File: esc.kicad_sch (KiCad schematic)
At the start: 49 parts, among them Q10 NMOS, Q5 NMOS, Q6 NMOS, Q7 NMOS, Q8 NMOS, Q9 NMOS, U16 DRV8328ARUYR, U20 STM32G071GBU6

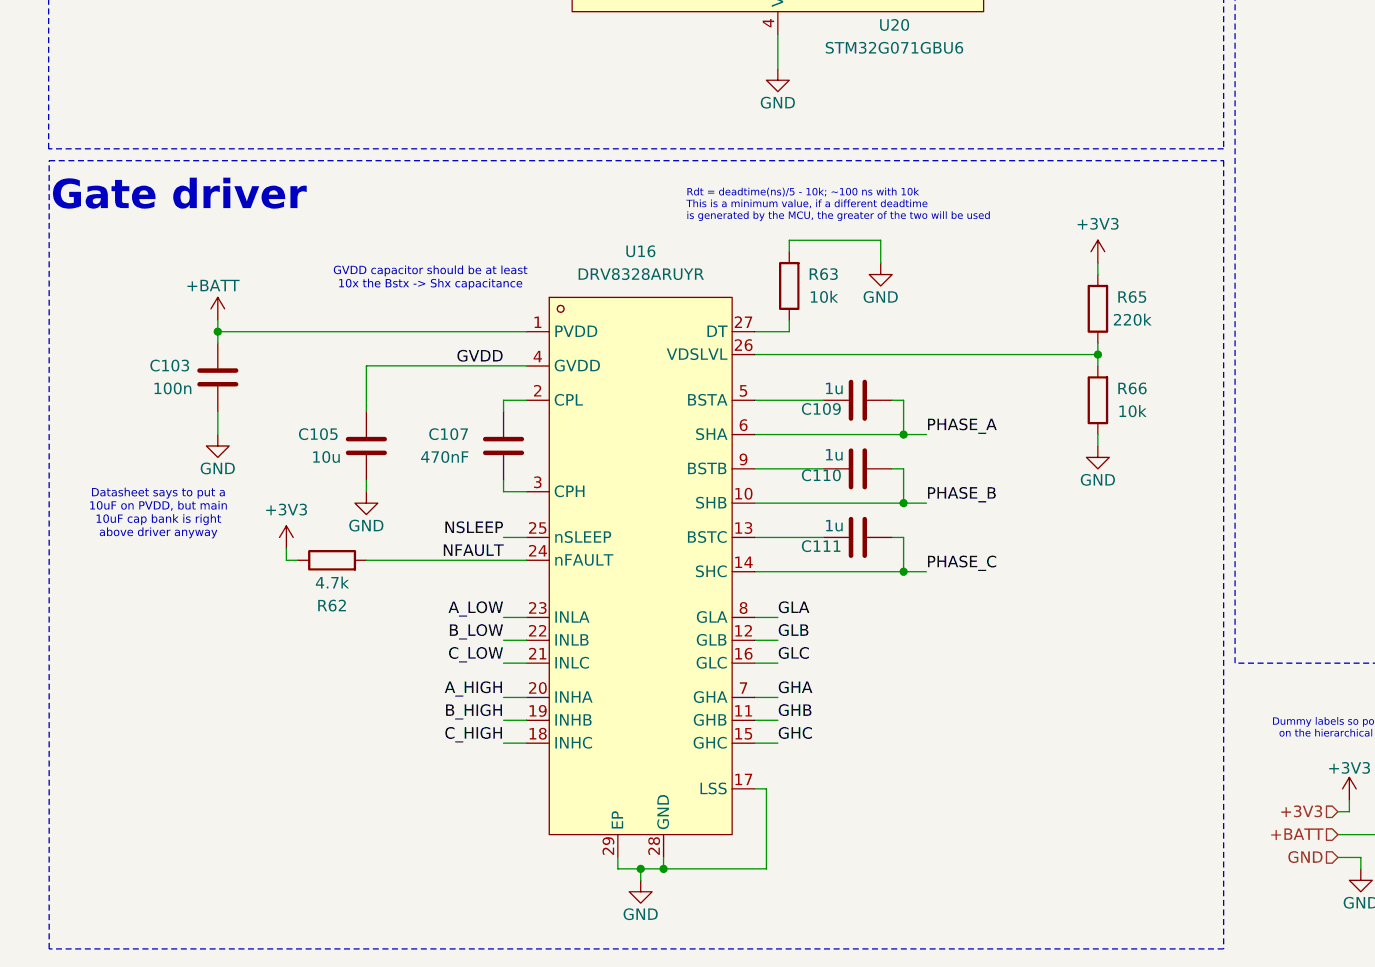
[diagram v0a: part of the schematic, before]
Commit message: Switch to 2.2 uH 1008 inductor for both DCDC converters
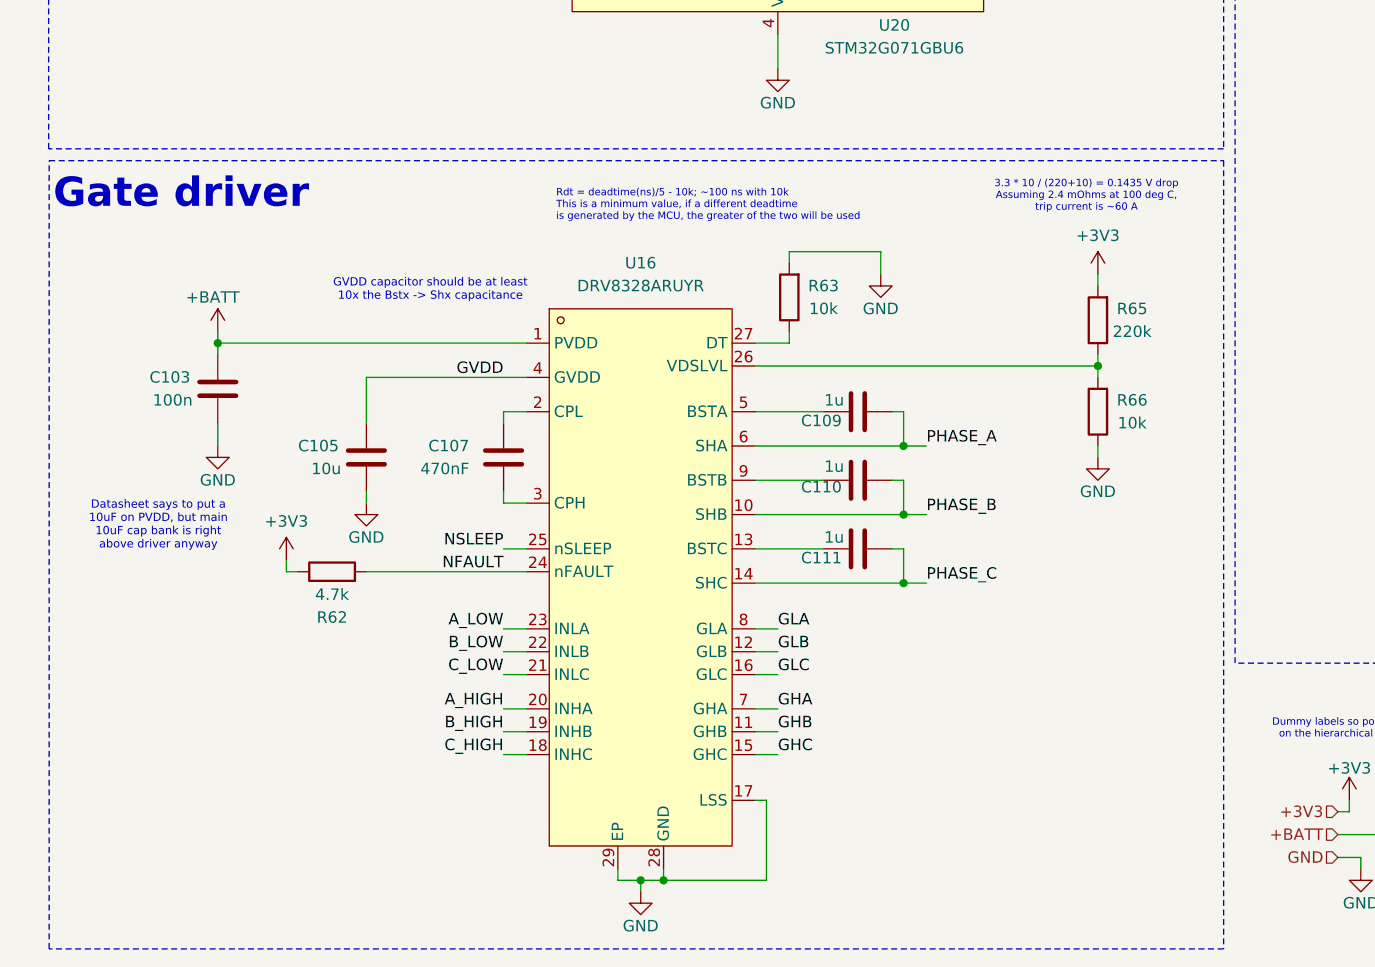
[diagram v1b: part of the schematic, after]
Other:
- note added: "3.3 * 10 / (220+10) = 0.1435 V drop Assuming 2.4 mOhms at 100 deg C, trip current is ~60 A"
- moved on the sheet: C103, C105, C107, C109, C110, C111, R62, R63, R65, R66, U16

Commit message: Fill out most of BOM
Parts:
- C107: LCSC Part (none) -> C576436
- D14: LCSC Part (none) -> C5440628
- Q10, Q5, Q6, Q7, Q8, Q9: LCSC Part (none) -> C2890409
- R136, R62: LCSC Part (none) -> C270346
- R139, R76, R79, R84: LCSC Part (none) -> C270365
- R63, R66, R75, R77, R78, R80, R83, R85: LCSC Part (none) -> C473048
- R65: LCSC Part (none) -> C473458
- R69, R70, R73, R74, R81, R82: LCSC Part (none) -> C270817

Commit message: Finish BOM list
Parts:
- C103: LCSC Part (none) -> C307331
- C105: LCSC Part (none) -> C237493
- C109, C110, C111, C180: LCSC Part (none) -> C52923
- C176, C178: LCSC Part (none) -> C76939

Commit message: Rename project
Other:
- title: Anticopter Duo -> P4eregrine

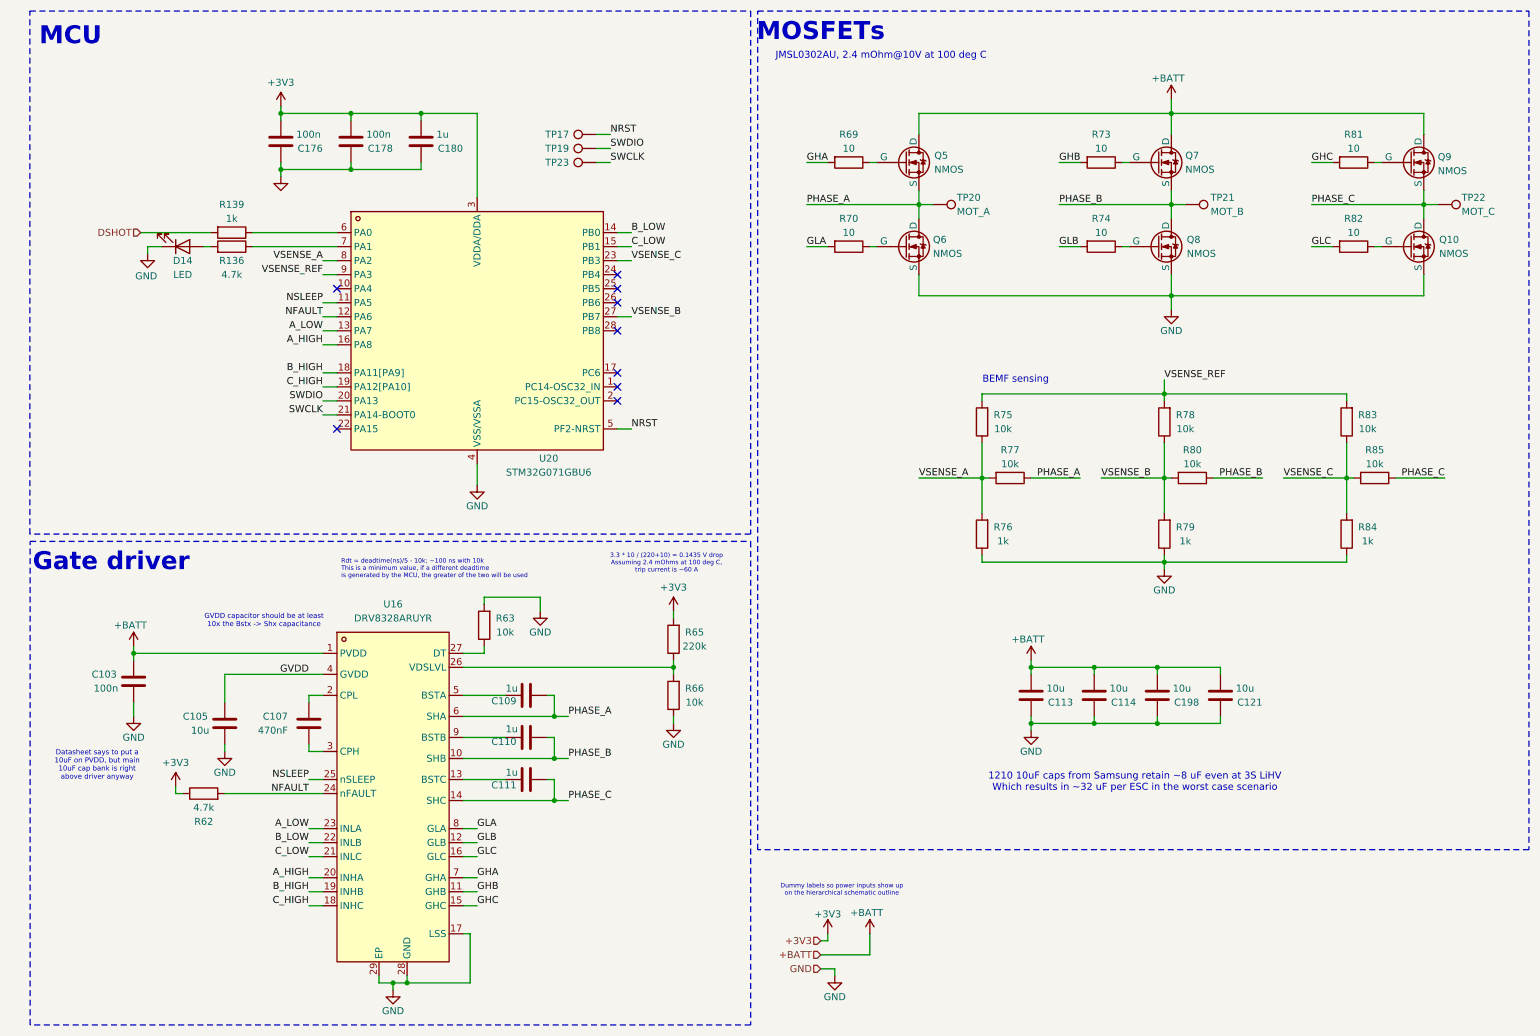
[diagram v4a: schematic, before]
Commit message: Remove redundant 100n STM cap
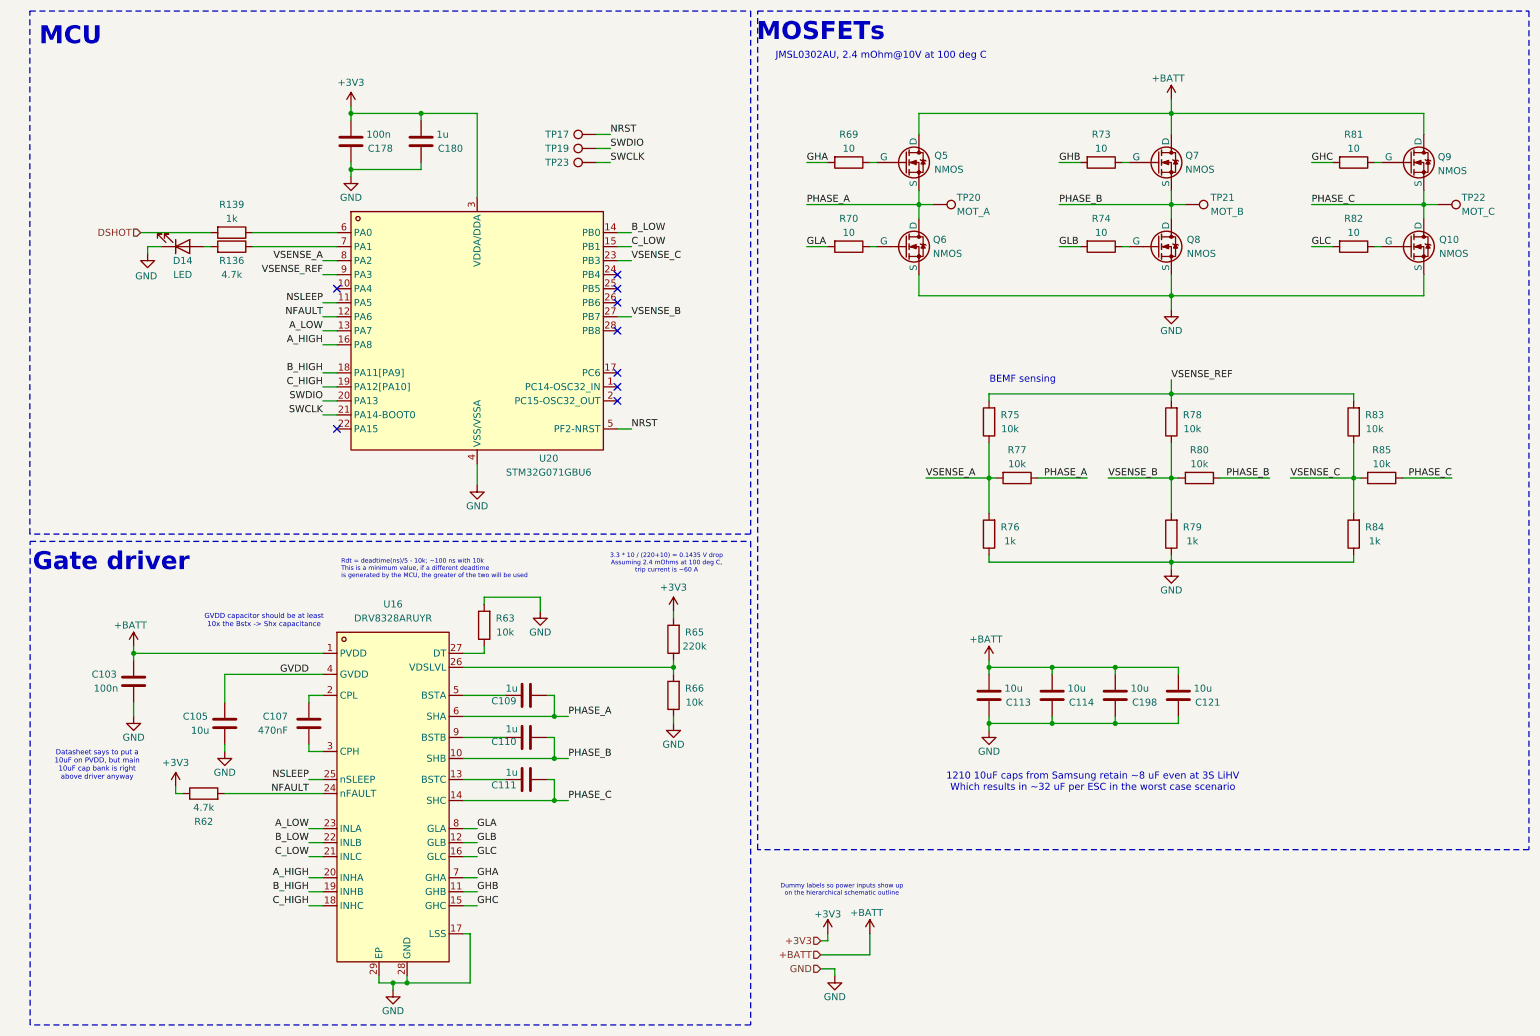
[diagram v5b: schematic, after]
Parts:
- removed C176: 100n, Capacitor_SMD:C_0201_0603Metric, symbol Device:C
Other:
- moved on the sheet: C113, C114, C121, C198, R75, R76, R77, R78, R79, R80, R83, R84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

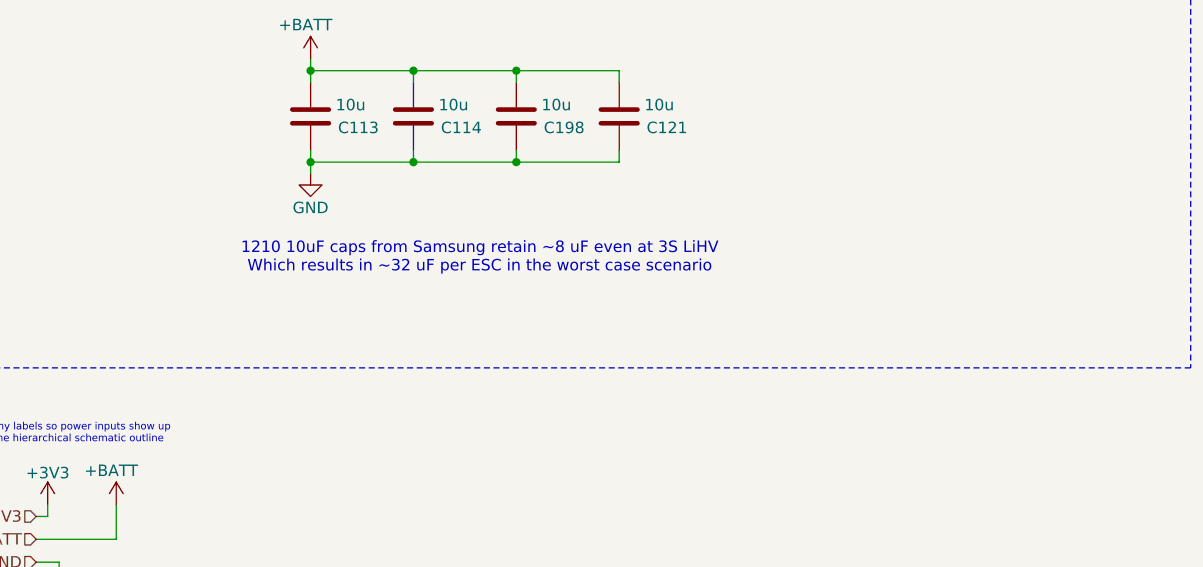
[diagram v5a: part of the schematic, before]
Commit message: Make GND probe pads square
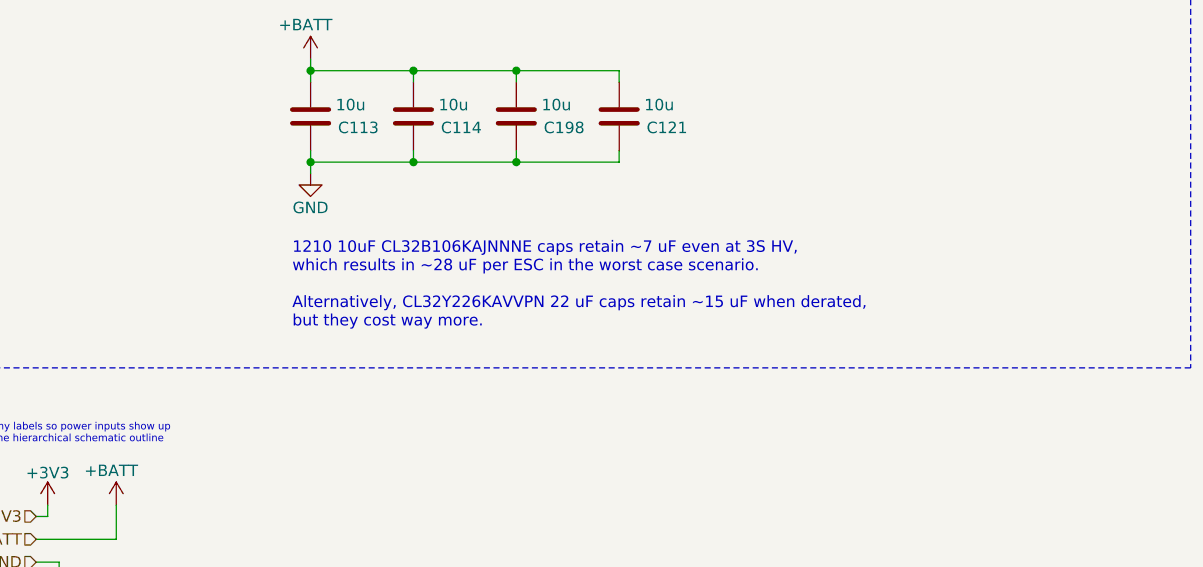
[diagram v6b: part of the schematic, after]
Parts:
- C113, C114, C121, C198: LCSC Part (none) -> C39232
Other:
- note added: "1210 10uF CL32B106KAJNNNE caps retain ~7 uF even at 3S HV, which results in ~28 uF per ESC in the worst case scenario. Alternatively, CL32Y226KAVVPN 22 uF caps retain ~15 uF when derated, but they cost way more."
- note removed: "1210 10uF caps from Samsung retain ~8 uF even at 3S LiHV Which results in ~32 uF per ESC in the worst case scenario"
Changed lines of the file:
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@@
 		)
 	)
-	(text "1210 10uF caps from Samsung retain ~8 uF even at 3S LiHV\nWhich results in ~32 uF per ESC in the worst case scenario"
+	(text "1210 10uF CL32B106KAJNNNE caps retain ~7 uF even at 3S HV, \nwhich results in ~28 uF per ESC in the worst case scenario.\n\nAlternatively, CL32Y226KAVVPN 22 uF caps retain ~15 uF when derated, \nbut they cost way more."
 		(exclude_from_sim no)
-		(at 205.486 152.908 0)
+		(at 184.658 155.956 0)
 		(effects
 			(font
 				(size 1.27 1.27)
 			)
+			(justify left)
 		)
 	)
@@
 			)
 		)
+		(property "LCSC Part" "C39232"
+			(at 186.69 137.16 0)
+			(hide yes)
+			(show_name no)
+			(do_not_autoplace no)
+			(effects
+				(font
+					(size 1.27 1.27)
+				)
+			)
+		)
 		(pin "1"
 		)
@@
 			)
 		)
+		(property "LCSC Part" "C39232"
+			(at 198.12 137.16 0)
+			(hide yes)
+			(show_name no)
+			(do_not_autoplace no)
+			(effects
+				(font
+					(size 1.27 1.27)
+				)
+			)
+		)
 		(pin "1"
 		)
@@
 			)
 		)
+		(property "LCSC Part" "C39232"
+			(at 220.98 137.16 0)
+			(hide yes)
+			(show_name no)
+			(do_not_autoplace no)
+			(effects
+				(font
+					(size 1.27 1.27)
+				)
+			)
+		)
 		(pin "1"
 		)
@@
 			(at 209.55 137.16 0)
 			(hide yes)
+			(show_name no)
+			(do_not_autoplace no)
+			(effects
+				(font
+					(size 1.27 1.27)
+				)
+			)
+		)
+		(property "LCSC Part" "C39232"
+			(at 209.55 137.16 0)
+			(hide yes)

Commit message: Adjust readme
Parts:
- TP17, TP19, TP20, TP21, TP22, TP23: now left out of the parts list
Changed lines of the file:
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@@
 		(body_style 1)
 		(exclude_from_sim no)
-		(in_bom yes)
+		(in_bom no)
 		(on_board yes)
-		(in_pos_files yes)
+		(in_pos_files no)
 		(dnp no)
 		(property "Reference" "TP22"
@@
 		(body_style 1)
 		(exclude_from_sim no)
-		(in_bom yes)
+		(in_bom no)
 		(on_board yes)
-		(in_pos_files yes)
+		(in_pos_files no)
 		(dnp no)
 		(property "Reference" "TP23"
@@
 		(body_style 1)
 		(exclude_from_sim no)
-		(in_bom yes)
+		(in_bom no)
 		(on_board yes)
-		(in_pos_files yes)
+		(in_pos_files no)
 		(dnp no)
 		(property "Reference" "TP19"
@@
 		(body_style 1)
 		(exclude_from_sim no)
-		(in_bom yes)
+		(in_bom no)
 		(on_board yes)
-		(in_pos_files yes)
+		(in_pos_files no)
 		(dnp no)
 		(property "Reference" "TP21"
@@
 		(body_style 1)
 		(exclude_from_sim no)
-		(in_bom yes)
+		(in_bom no)
 		(on_board yes)
-		(in_pos_files yes)
+		(in_pos_files no)
 		(dnp no)
 		(property "Reference" "TP20"
@@
 		(body_style 1)
 		(exclude_from_sim no)
-		(in_bom yes)
+		(in_bom no)
 		(on_board yes)
-		(in_pos_files yes)
+		(in_pos_files no)
 		(dnp no)
 		(property "Reference" "TP17"

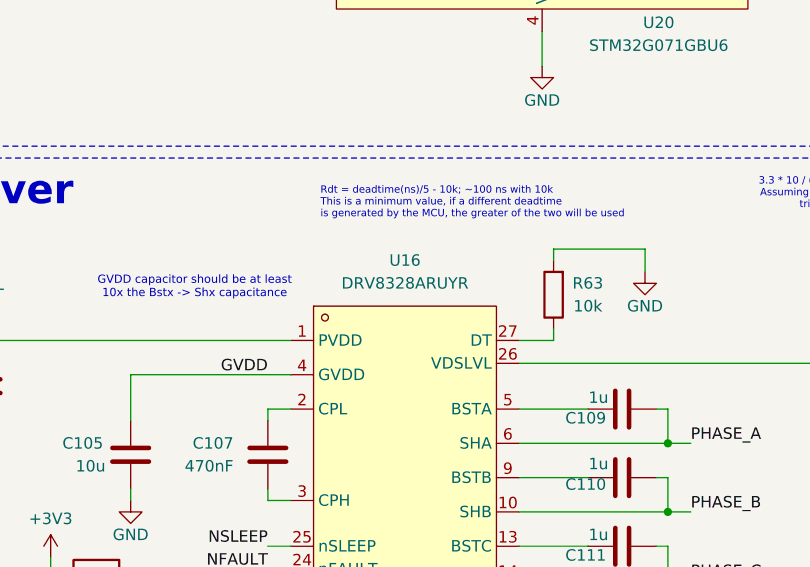
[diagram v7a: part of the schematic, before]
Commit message: Get rid of 4.7uf caps and add missing MPNs to BOM
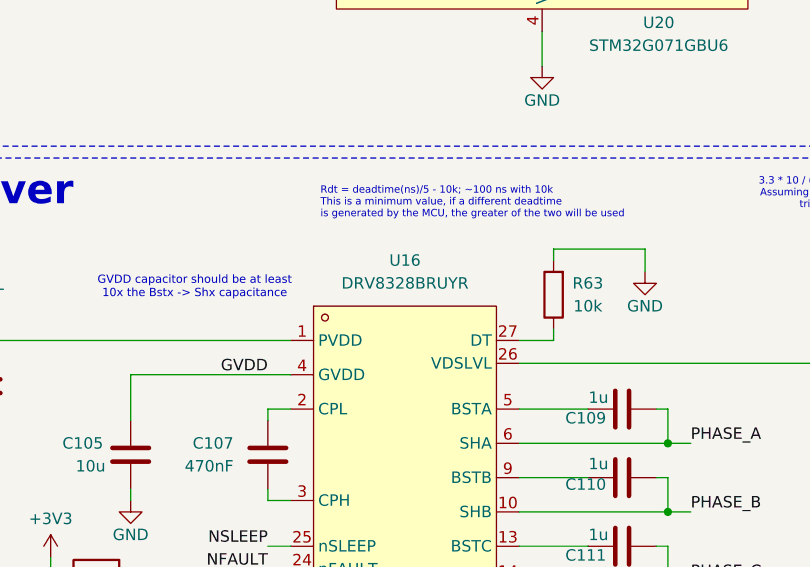
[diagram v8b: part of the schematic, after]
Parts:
- C103: MPN (none) -> CL05B104KB54PNC
- C105: MPN (none) -> GRM21BZ71E106KE15L
- C107: LCSC Part C576436 -> C437527; MPN (none) -> GRM155R61H474KE11D
- C109, C110, C111, C180: MPN (none) -> CL05A105KA5NQNC
- C113, C114, C121, C198: MPN (none) -> CL32B106KAJNNNE
- C178: MPN (none) -> GRM033R61E104KE14D
- D14: MPN (none) -> XL-0201UYC
- Q10, Q5, Q6, Q7, Q8, Q9: MPN (none) -> JMSL0302AU
- R136, R62: MPN (none) -> 0201WMF4701TEE
- R139, R76, R79, R84: MPN (none) -> 0201WMF1001TEE
- R63, R66, R75, R77, R78, R80, R83, R85: MPN (none) -> 0201WMF1002TEE
- R65: MPN (none) -> 0201WMF2203TEE
- R69, R70, R73, R74, R81, R82: MPN (none) -> 0201WMF100JTEE
- U16: value DRV8328ARUYR -> DRV8328BRUYR
